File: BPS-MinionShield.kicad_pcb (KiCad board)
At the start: 2 copper layers, 85 x 66 mm, 81 parts, among them J1 TempConn1, J2 TempConn2, J3 Conn_01x24_Female

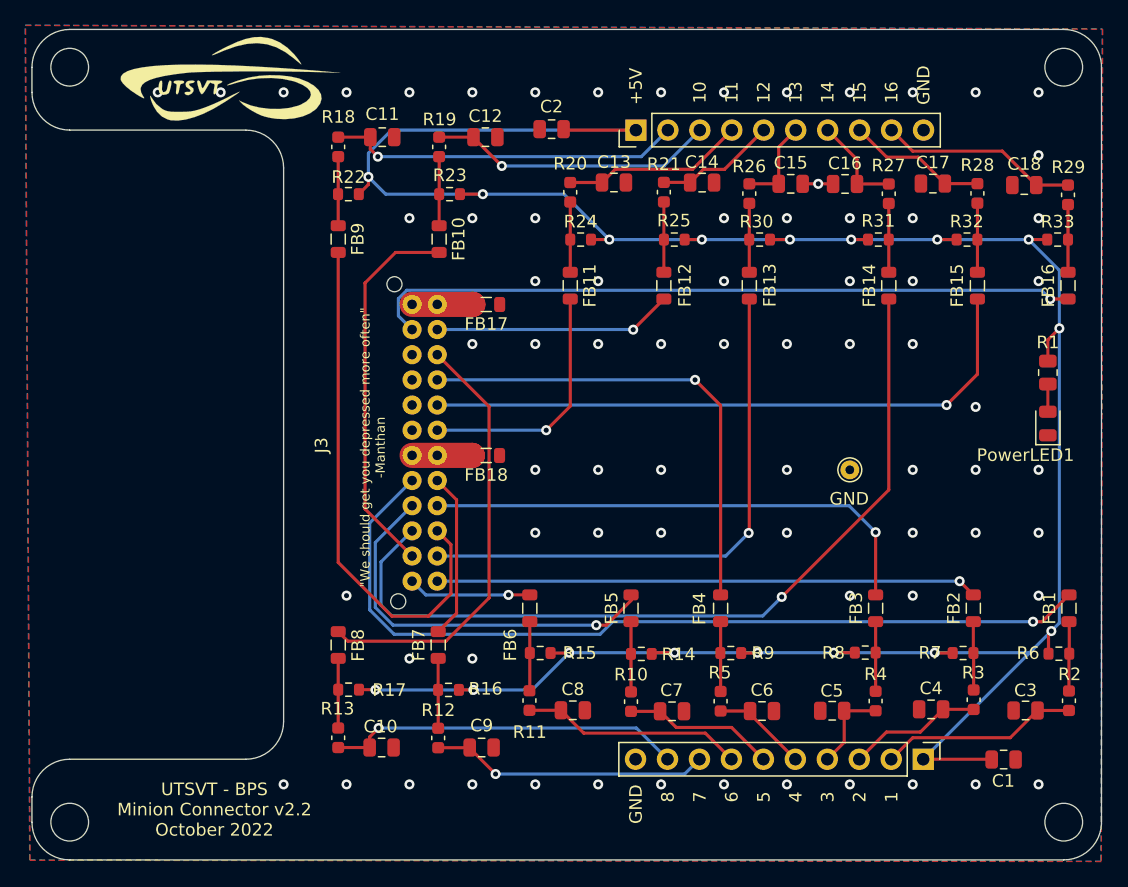
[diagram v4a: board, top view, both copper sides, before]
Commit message: move ferrite beads for more space
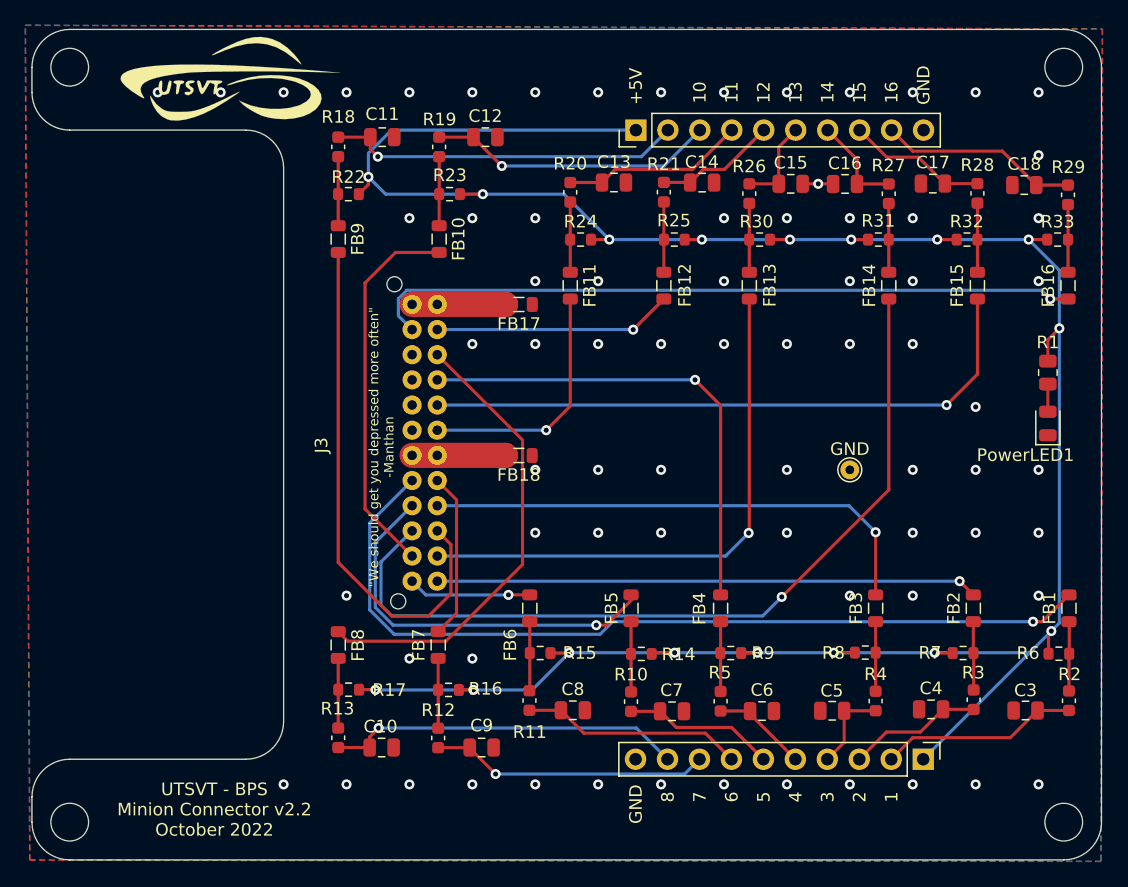
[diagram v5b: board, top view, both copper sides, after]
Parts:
- removed C1, C2: 100n, Capacitor_SMD:C_0805_2012Metric
- moved FB18 2.59 mm to (138.7, 103.9)
- moved FB17 2.59 mm to (138.7, 91.9)
- turned GND to 0 degrees
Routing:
- net +5V: track 217.0 -> 205.8 mm
- net Net-(FB18-Pad2): track 4.81 -> 7.42 mm
- net Net-(FB17-Pad2): track 4.84 -> 7.43 mm
- net /temp14: track 34.8 -> 37.0 mm

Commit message: Revert "move ferrite beads for more space"
This reverts commit 10398d522d6bd349285b691c333d995223f13479.
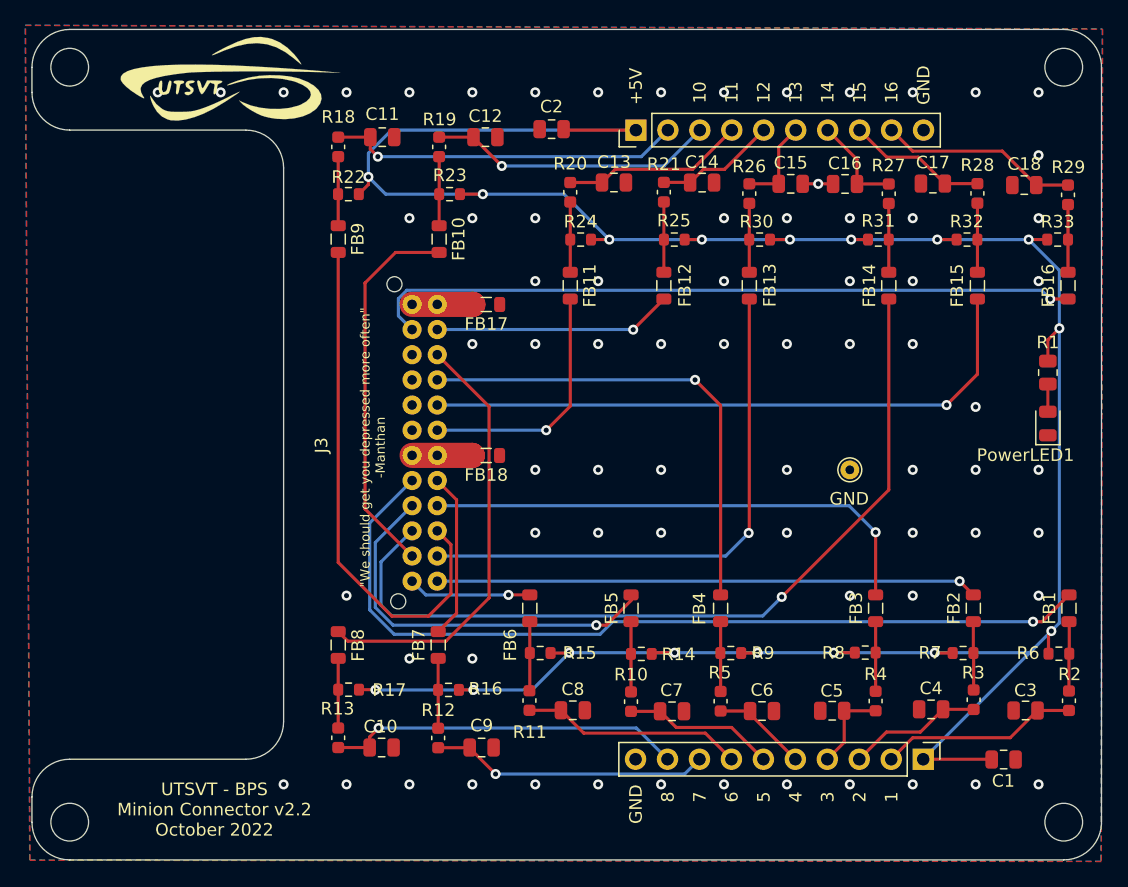
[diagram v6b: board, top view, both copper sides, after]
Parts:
- added C1: 100n, Capacitor_SMD:C_0805_2012Metric, F.Cu at (177.2, 128.0)
- added C2: 100n, Capacitor_SMD:C_0805_2012Metric, F.Cu at (141.3, 77.9)
- moved FB18 2.59 mm to (136.1, 103.9)
- moved FB17 2.59 mm to (136.1, 91.9)
- turned GND to 180 degrees
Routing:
- net +5V: track 205.8 -> 217.0 mm
- net Net-(FB18-Pad2): track 7.42 -> 4.81 mm
- net Net-(FB17-Pad2): track 7.43 -> 4.84 mm
- net /temp14: track 37.0 -> 34.8 mm

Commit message: fix footprints and reference designators
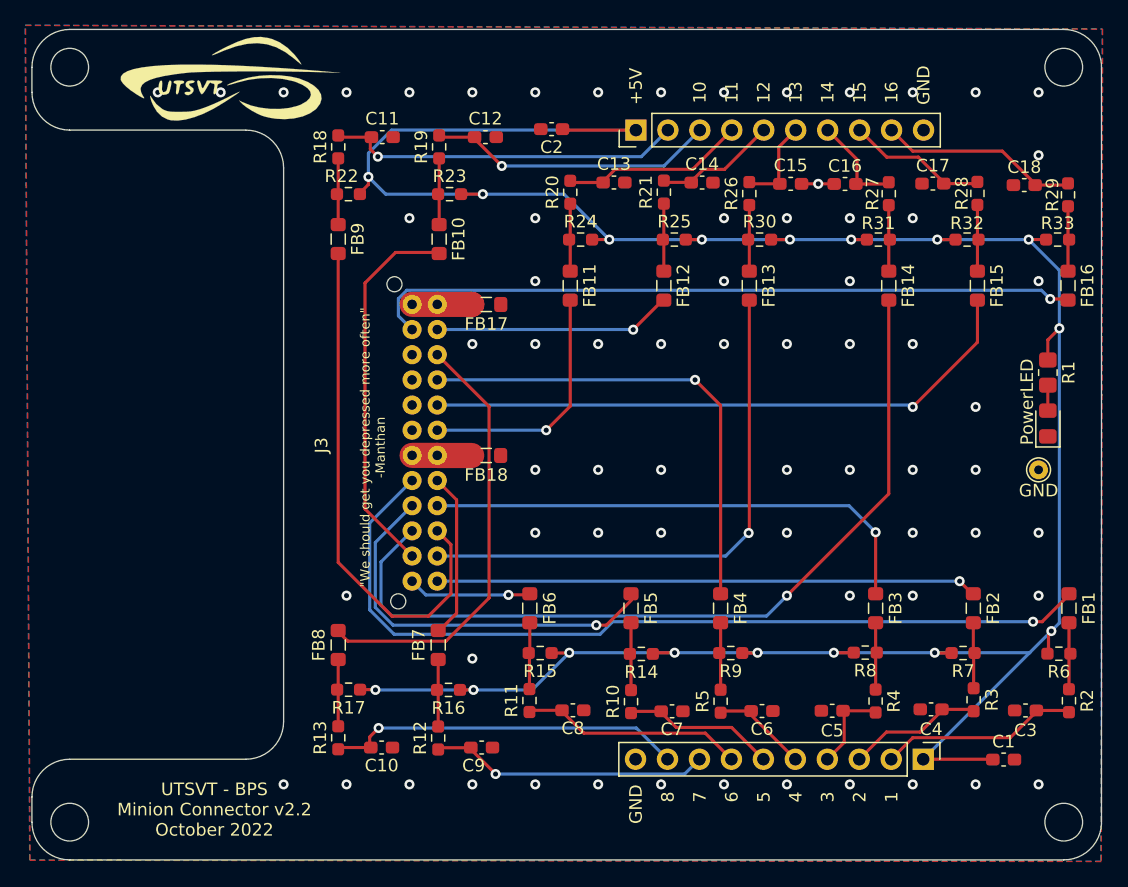
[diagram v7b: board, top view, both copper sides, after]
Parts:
- C1, C2: value 100n -> 1u; footprint Capacitor_SMD:C_0805_2012Metric -> Capacitor_SMD:C_0603_1608Metric_Pad1.08x0.95mm_HandSolder
- C10, C11, C12, C13, C14, C15, C16, C17, C18, C3, C4, C5, C6, C7, C8, C9: footprint Capacitor_SMD:C_0805_2012Metric -> Capacitor_SMD:C_0603_1608Metric_Pad1.08x0.95mm_HandSolder
- FB1, FB10, FB11, FB12, FB13, FB14, FB15, FB16, FB17, FB18, FB2, FB3, FB4, FB5, FB6, FB7, FB8, FB9: footprint Inductor_SMD:L_0805_2012Metric -> Inductor_SMD:L_0805_2012Metric_Pad1.05x1.20mm_HandSolder
- PowerLED: renamed from PowerLED1; footprint LED_SMD:LED_0805_2012Metric -> LED_SMD:LED_0805_2012Metric_Pad1.15x1.40mm_HandSolder
- R1: footprint Resistor_SMD:R_0805_2012Metric -> Resistor_SMD:R_0805_2012Metric_Pad1.20x1.40mm_HandSolder
- R10, R11, R12, R13, R18, R19, R2, R20, R21, R26, R27, R28, R29, R3, R4, R5: footprint Capacitor_SMD:C_0603_1608Metric -> Resistor_SMD:R_0603_1608Metric_Pad0.98x0.95mm_HandSolder
- R14, R15, R16, R17, R22, R23, R24, R25, R30, R31, R32, R33, R6, R7, R8, R9: footprint Resistor_SMD:R_0603_1608Metric -> Resistor_SMD:R_0603_1608Metric_Pad0.98x0.95mm_HandSolder
- moved GND 15.0 mm to (180.0, 105.0)
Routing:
- net /temp12: track 49.9 -> 48.5 mm
- net GND: vias 73 -> 68

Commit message: change to all passives to 0805 footprints
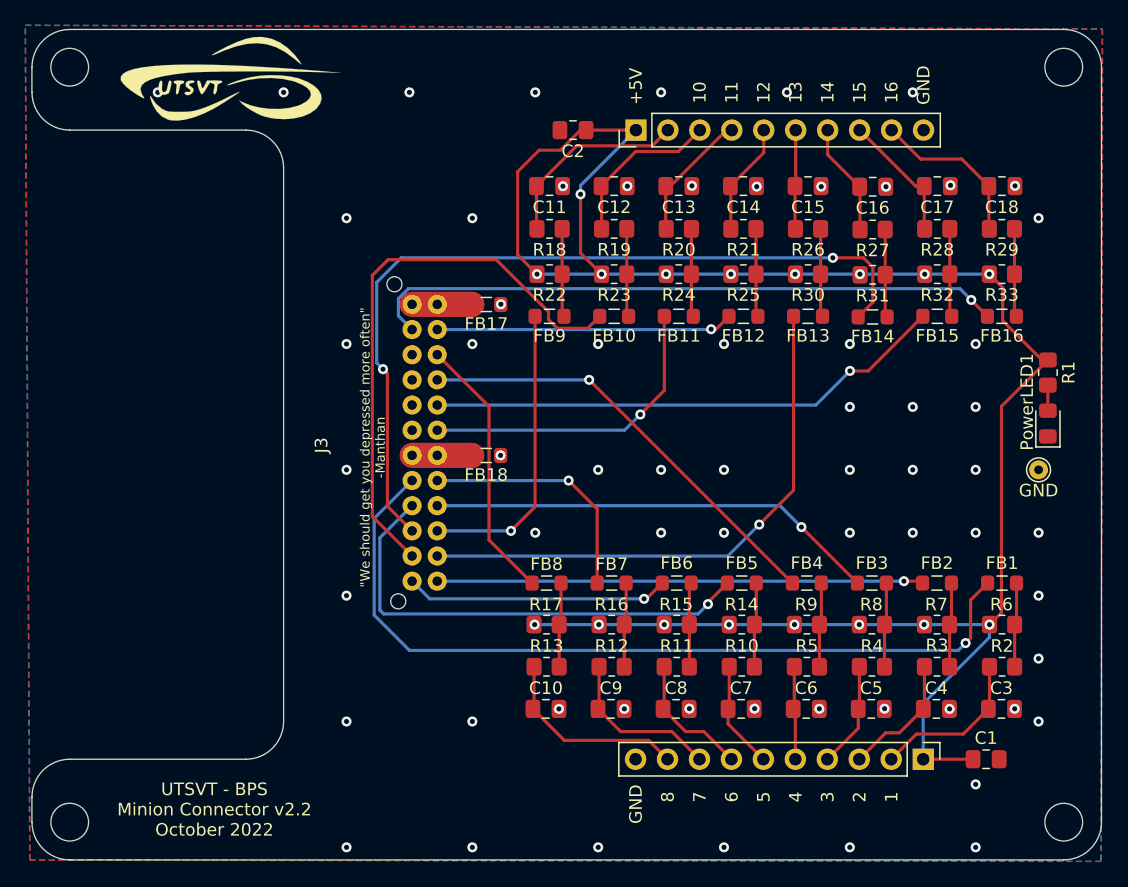
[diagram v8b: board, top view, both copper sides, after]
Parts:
- C1, C10, C11, C12, C13, C14, C15, C16, C17, C18, C2, C3, C4, C5, C6, C7, C8, C9: footprint Capacitor_SMD:C_0603_1608Metric_Pad1.08x0.95mm_HandSolder -> Capacitor_SMD:C_0805_2012Metric_Pad1.18x1.45mm_HandSolder
- R10, R11, R12, R13, R14, R15, R16, R17, R18, R19, R2, R20, R21, R22, R23, R24, R25, R26, R27, R28, R29, R3, R30, R31, R32, R33, R4, R5, R6, R7, R8, R9: footprint Resistor_SMD:R_0603_1608Metric_Pad0.98x0.95mm_HandSolder -> Resistor_SMD:R_0805_2012Metric_Pad1.20x1.40mm_HandSolder
- moved R18 18.0 mm to (141.1, 85.8), turned to 0 degrees
- moved FB9 17.9 mm to (141.1, 92.8), turned to 180 degrees
- moved R13 17.5 mm to (140.9, 120.7), turned to 0 degrees
- moved FB8 17.3 mm to (140.9, 114.0), turned to 180 degrees
- moved R22 17.2 mm to (141.1, 89.5), turned to 180 degrees
- moved R17 16.6 mm to (140.9, 117.3), turned to 180 degrees
- moved R19 15.4 mm to (146.3, 85.8), turned to 0 degrees
- moved FB10 15.2 mm to (146.3, 92.8), turned to 180 degrees
- moved R12 14.9 mm to (146.1, 120.7), turned to 0 degrees
- moved FB7 14.6 mm to (146.1, 114.0), turned to 180 degrees
- moved R23 14.5 mm to (146.3, 89.5), turned to 180 degrees
- moved R16 14.0 mm to (146.1, 117.3), turned to 180 degrees
- moved C11 13.9 mm to (141.1, 82.5)
- moved C10 13.4 mm to (140.8, 124.0)
- moved R11 12.0 mm to (151.2, 120.7), turned to 0 degrees
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- renumbered PowerLED to PowerLED1
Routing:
- net +5V: track 217.0 -> 154.4 mm
- net /temp3: track 41.5 -> 23.7 mm, vias 0 -> 1
- net /temp7: track 30.1 -> 45.2 mm
- net /temp14: track 34.8 -> 21.3 mm
- net /TempSens8: track 28.3 -> 15.7 mm, vias 1 -> 0
- net /TempSens9: track 28.3 -> 15.7 mm, vias 1 -> 0
- net /temp6: track 9.81 -> 21.0 mm
- net /TempSens10: track 22.9 -> 13.1 mm, vias 1 -> 0
- net /TempSens7: track 22.2 -> 13.1 mm, vias 1 -> 0
- net /TempSens6: track 17.7 -> 10.5 mm
- net /temp12: track 48.5 -> 41.5 mm
- net /temp2: track 31.5 -> 38.2 mm
- net /temp10: track 13.2 -> 19.5 mm, vias 0 -> 1
- net /temp16: track 56.7 -> 51.0 mm
- net /temp11: track 19.9 -> 25.2 mm
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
